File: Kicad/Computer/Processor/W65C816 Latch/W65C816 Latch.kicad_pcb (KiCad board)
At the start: 2 copper layers, 18.8 x 17.9 mm, 11 parts, among them IC1 74LVC08APW,112, J2 Board 2x06 W15.24mm

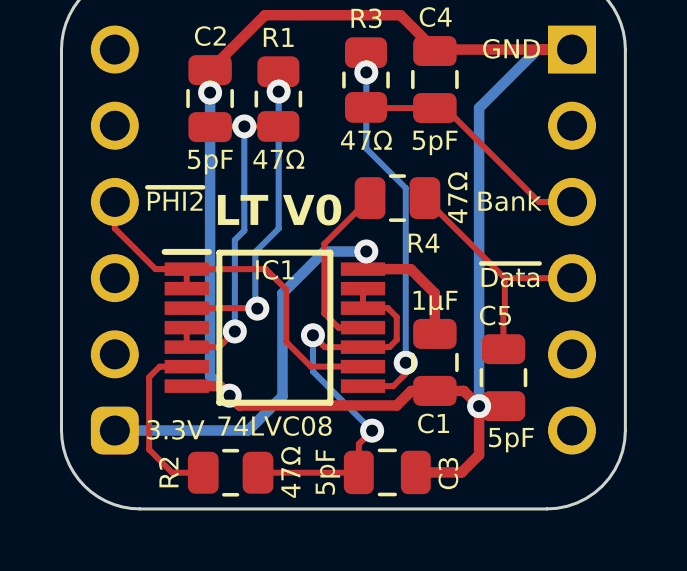
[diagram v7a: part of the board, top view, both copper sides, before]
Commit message: Added a board presence reader to the Processor Board.
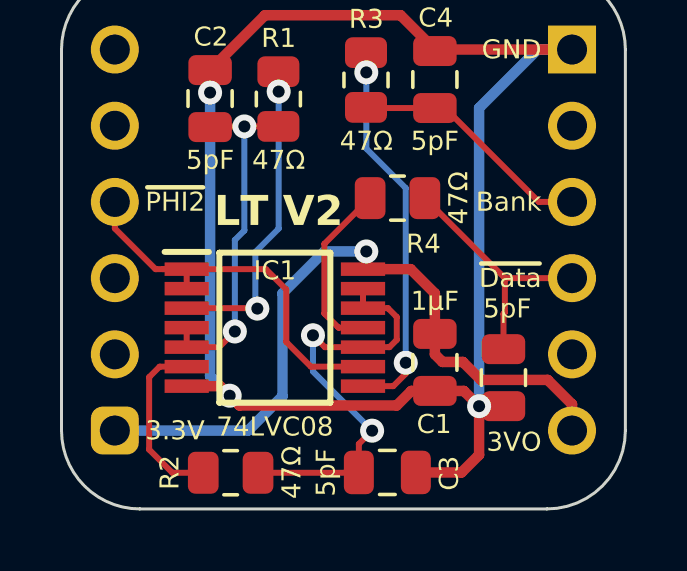
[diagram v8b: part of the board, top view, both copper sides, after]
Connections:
- J2 pad 7: unconnected-(J2-Pad7) -> 3.3V
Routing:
- net 3.3V: track 17.4 -> 24.2 mm
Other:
- board text added: "3VO"
- board text added: "LT V2"
- board text removed: "LT V0"
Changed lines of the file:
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@@
 	(title_block
 		(title "MPU Timer")
-		(date "2024-02-22")
-		(rev "V1")
+		(date "2026-01-29")
+		(rev "V2")
 	)
 	(layers
@@
 	(net 11 "Net-(IC1-1Y)")
 	(net 12 "unconnected-(J2-Pad5)")
-	(net 13 "unconnected-(J2-Pad7)")
-	(net 14 "unconnected-(J2-Pad1)")
-	(net 15 "unconnected-(J2-Pad11)")
-	(net 16 "unconnected-(J2-Pad8)")
-	(net 17 "unconnected-(J2-Pad2)")
-	(net 18 "unconnected-(J2-Pad4)")
+	(net 13 "unconnected-(J2-Pad1)")
+	(net 14 "unconnected-(J2-Pad11)")
+	(net 15 "unconnected-(J2-Pad8)")
+	(net 16 "unconnected-(J2-Pad2)")
+	(net 17 "unconnected-(J2-Pad4)")
 	(footprint "SamacSys_Parts:R_0805"
 		(layer "F.Cu")
@@
 			(at 0.254 2.032 0)
 			(layer "F.SilkS")
+			(hide yes)
 			(effects
 				(font
@@
 		)
 		(property "Value" "5pF"
-			(at -0.254 -2.032 0)
+			(at -0.127 2.286 0)
 			(layer "F.SilkS")
 			(effects
@@
 			(layers "*.Cu" "*.Mask")
 			(remove_unused_layers no)
-			(net 14 "unconnected-(J2-Pad1)")
+			(net 13 "unconnected-(J2-Pad1)")
 			(pintype "passive+no_connect")
 		)
@@
 			(layers "*.Cu" "*.Mask")
 			(remove_unused_layers no)
-			(net 17 "unconnected-(J2-Pad2)")
+			(net 16 "unconnected-(J2-Pad2)")
 			(pintype "passive+no_connect")
 		)
@@
 			(layers "*.Cu" "*.Mask")
 			(remove_unused_layers no)
-			(net 18 "unconnected-(J2-Pad4)")
+			(net 17 "unconnected-(J2-Pad4)")
 			(pintype "passive+no_connect")
 		)
@@
 			(layers "*.Cu" "*.Mask")
 			(remove_unused_layers no)
-			(net 13 "unconnected-(J2-Pad7)")
-			(pintype "passive+no_connect")
+			(net 2 "3.3V")
+			(pintype "passive")
 		)
 		(pad "8" thru_hole oval
@@
 			(layers "*.Cu" "*.Mask")
 			(remove_unused_layers no)
-			(net 16 "unconnected-(J2-Pad8)")
+			(net 15 "unconnected-(J2-Pad8)")
 			(pintype "passive+no_connect")
 		)
@@
 			(layers "*.Cu" "*.Mask")
 			(remove_unused_layers no)
-			(net 15 "unconnected-(J2-Pad11)")
+			(net 14 "unconnected-(J2-Pad11)")
 			(pintype "passive+no_connect")
 		)
@@
 		)
 	)
+	(gr_text "3VO"
+		(at 14.224 13.081 0)
+		(layer "F.SilkS")
+		(effects
+			(font
+				(size 0.635 0.635)
+				(thickness 0.15)
+			)
+			(justify right)
+		)
+	)
 	(gr_text "GND"
 		(at 14.224 0 0)
@@
 		)
 	)
-	(gr_text "LT V0"
+	(gr_text "LT V2"
 		(at 5.461 5.969 0)
 		(layer "F.SilkS" knockout)
@@
 	)
 	(segment
+		(start 10.922 10.414)
+		(end 11.602 10.414)
+		(width 0.35)
+		(layer "F.Cu")
+		(net 2)
+	)
+	(segment
 		(start 10.668 8.128)
 		(end 10.668 9.48)
@@
 	)
 	(segment
+		(start 11.602 10.414)
+		(end 12.2 11.012)
+		(width 0.35)
+		(layer "F.Cu")
+		(net 2)
+	)
+	(segment
+		(start 14.428884 11.012)
+		(end 15.24 11.823116)
+		(width 0.35)
+		(layer "F.Cu")
+		(net 2)
+	)
+	(segment
+		(start 10.668 9.48)
+		(end 10.668 10.16)
+		(width 0.35)
+		(layer "F.Cu")
+		(net 2)
+	)
+	(segment
+		(start 12.2 11.012)
+		(end 14.428884 11.012)
+		(width 0.35)
+		(layer "F.Cu")
+		(net 2)
+	)
+	(segment
+		(start 15.24 11.823116)
+		(end 15.24 12.7)
+		(width 0.35)
+		(layer "F.Cu")
+		(net 2)
+	)
+	(segment
 		(start 8.3823 7.321)
 		(end 9.861 7.321)
 		(width 0.35)
 		(layer "F.Cu")
+		(net 2)
+	)
+	(segment
+		(start 10.668 10.16)
+		(end 10.922 10.414)
+		(width 0.35)
+		(layer "F.Cu")
